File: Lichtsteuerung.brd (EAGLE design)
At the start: 157.7 x 86.4 mm, 137 parts, among them IC1 74HC595D, IC10 TSR_1-2450, IC11 MEGA64-A, IC12 75176AD, IC13 DS1307SO8, IC2 74HC595D, IC3 74HC595D, IC4 74HC595D, IC5 75176AD, IC6 MEGA8-AI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

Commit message: Added another aux connector to supply SDA, SCL, +5V and GND
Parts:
- added JP4: (no value), pinhead:2X03
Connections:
- new net AUXCON_23: IC11.5, JP4.5
- new net AUXCON_24: IC11.4, JP4.6
- net +5V: now also JP4.3
- net GND: now also JP4.4
- net SCL: now also JP4.2
- net SDA: now also JP4.1
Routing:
- net AUXCON_24: track 0.00 -> 32.9 mm
- net AUXCON_23: track 0.00 -> 30.7 mm
- net SDA: track 158.7 -> 181.2 mm
- net SCL: track 165.9 -> 185.8 mm
- net +5V: track 525.4 -> 535.2 mm
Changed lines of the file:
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@@
 <setting verticaltext="up"/>
 </settings>
-<grid distance="0.254" unitdist="mm" unit="mm" style="lines" multiple="5" display="yes" altdistance="1.27" altunitdist="mm" altunit="mm"/>
+<grid distance="0.254" unitdist="mm" unit="mil" style="lines" multiple="5" display="yes" altdistance="1.27" altunitdist="mm" altunit="mm"/>
 <layers>
 <layer number="1" name="Top" color="4" fill="1" visible="no" active="yes"/>
@@
 <text x="7.7" y="4.2" size="1.016" layer="25" rot="R90">Digital Outputs</text>
 <text x="60.9" y="4.2" size="1.016" layer="25" rot="R90">Digital Outputs</text>
-<rectangle x1="106.688" y1="27.868" x2="107.038" y2="29.268" layer="25" rot="R180"/>
-<rectangle x1="96.538" y1="31.718" x2="96.888" y2="33.118" layer="25" rot="R180"/>
-<rectangle x1="101.088" y1="30.318" x2="101.438" y2="30.668" layer="25" rot="R180"/>
-<rectangle x1="102.488" y1="25.768" x2="103.538" y2="26.118" layer="25" rot="R180"/>
-<rectangle x1="102.488" y1="26.118" x2="102.838" y2="26.818" layer="25" rot="R180"/>
-<rectangle x1="102.838" y1="26.468" x2="103.538" y2="26.818" layer="25" rot="R180"/>
-<rectangle x1="103.188" y1="26.818" x2="103.538" y2="27.518" layer="25" rot="R180"/>
-<rectangle x1="102.488" y1="27.168" x2="103.188" y2="27.518" layer="25" rot="R180"/>
-<rectangle x1="101.438" y1="26.118" x2="101.788" y2="26.468" layer="25" rot="R180"/>
-<rectangle x1="101.438" y1="26.818" x2="101.788" y2="27.168" layer="25" rot="R180"/>
-<rectangle x1="100.388" y1="25.768" x2="100.738" y2="27.518" layer="25" rot="R180"/>
-<rectangle x1="95.838" y1="24.718" x2="107.738" y2="25.068" layer="25" rot="R180"/>
-<rectangle x1="95.488" y1="34.168" x2="108.088" y2="34.518" layer="25" rot="R180"/>
-<rectangle x1="107.738" y1="24.718" x2="108.088" y2="34.168" layer="25" rot="R180"/>
-<rectangle x1="95.488" y1="24.718" x2="95.838" y2="34.168" layer="25" rot="R180"/>
+<rectangle x1="146.009" y1="35.043" x2="146.359" y2="36.443" layer="25" rot="R270"/>
+<rectangle x1="142.159" y1="24.893" x2="142.509" y2="26.293" layer="25" rot="R270"/>
+<rectangle x1="144.084" y1="29.968" x2="144.434" y2="30.318" layer="25" rot="R270"/>
+<rectangle x1="148.284" y1="31.718" x2="149.334" y2="32.068" layer="25" rot="R270"/>
+<rectangle x1="148.109" y1="31.193" x2="148.459" y2="31.893" layer="25" rot="R270"/>
+<rectangle x1="147.759" y1="31.893" x2="148.459" y2="32.243" layer="25" rot="R270"/>
+<rectangle x1="147.409" y1="31.893" x2="147.759" y2="32.593" layer="25" rot="R270"/>
+<rectangle x1="147.059" y1="31.543" x2="147.759" y2="31.893" layer="25" rot="R270"/>
+<rectangle x1="148.284" y1="30.318" x2="148.634" y2="30.668" layer="25" rot="R270"/>
+<rectangle x1="147.584" y1="30.318" x2="147.934" y2="30.668" layer="25" rot="R270"/>
+<rectangle x1="147.934" y1="28.568" x2="148.284" y2="30.318" layer="25" rot="R270"/>
+<rectangle x1="143.909" y1="30.493" x2="155.809" y2="30.843" layer="25" rot="R270"/>
+<rectangle x1="134.109" y1="30.493" x2="146.709" y2="30.843" layer="25" rot="R270"/>
+<rectangle x1="145.134" y1="32.068" x2="145.484" y2="41.518" layer="25" rot="R270"/>
+<rectangle x1="145.134" y1="19.818" x2="145.484" y2="29.268" layer="25" rot="R270"/>
 <rectangle x1="4.2" y1="37.1" x2="5.95" y2="37.45" layer="26"/>
 <rectangle x1="5.95" y1="36.75" x2="6.65" y2="37.1" layer="26"/>
@@
 <element name="F5" library="ptc-littlefuse" package="1812L" value="500mA" x="153" y="15" rot="MR270"/>
 <element name="C21" library="resistor" package="C0805" value="100n" x="135.636" y="42.164" rot="R180"/>
+<element name="JP4" library="pinhead" package="2X03" value="" x="97.79" y="27.94" rot="R270"/>
 </elements>
 <signals>
@@
 <via x="67.31" y="41.91" extent="1-16" drill="0.6"/>
 <contactref element="C21" pad="1"/>
+<contactref element="JP4" pad="4"/>
 </signal>
 <signal name="N$36">
@@
 <wire x1="134.874" y1="40.894" x2="134.874" y2="42.076" width="0.3048" layer="1"/>
 <wire x1="134.874" y1="42.076" x2="134.786" y2="42.164" width="0.3048" layer="1"/>
+<contactref element="JP4" pad="3"/>
+<wire x1="92.925" y1="34.925" x2="92.925" y2="29.249" width="0.4064" layer="1"/>
+<wire x1="92.925" y1="29.249" x2="94.234" y2="27.94" width="0.4064" layer="1"/>
+<wire x1="94.234" y1="27.94" x2="96.52" y2="27.94" width="0.4064" layer="1"/>
 </signal>
 <signal name="SR_SCK">
@@
 <wire x1="81.915" y1="44.7675" x2="81.362828125" y2="44.7675" width="0.3048" layer="16"/>
 <wire x1="81.362828125" y1="44.7675" x2="79.982103125" y2="46.148225" width="0.3048" layer="16"/>
-<wire x1="81.915" y1="44.7675" x2="86.36" y2="44.7675" width="0.3048" layer="16"/>
-<wire x1="86.36" y1="44.7675" x2="86.995" y2="43.815" width="0.3048" layer="16"/>
+<wire x1="81.915" y1="44.7675" x2="86.106" y2="44.7675" width="0.3048" layer="16"/>
+<wire x1="86.106" y1="44.7675" x2="86.995" y2="43.815" width="0.3048" layer="16"/>
 <wire x1="86.995" y1="43.815" x2="86.995" y2="40.9575" width="0.3048" layer="16"/>
 <via x="86.995" y="40.9575" extent="1-16" drill="0.6"/>
@@
 <wire x1="74.93" y1="52.3875" x2="74.93" y2="46.355" width="0.3048" layer="1"/>
 <wire x1="72.39" y1="47.625" x2="72.39" y2="48.26" width="0.3048" layer="1"/>
+<contactref element="JP4" pad="2"/>
+<wire x1="94.615" y1="48.5775" x2="94.615" y2="43.053" width="0.3048" layer="16"/>
+<wire x1="94.615" y1="43.053" x2="99.06" y2="38.608" width="0.3048" layer="16"/>
+<wire x1="99.06" y1="38.608" x2="99.06" y2="30.48" width="0.3048" layer="16"/>
 </signal>
 <signal name="SDA">
@@
 <wire x1="68.58" y1="51.7525" x2="67.945" y2="52.3875" width="0.3048" layer="1"/>
 <wire x1="67.945" y1="52.3875" x2="61.2775" y2="52.3875" width="0.3048" layer="1"/>
+<contactref element="JP4" pad="1"/>
+<wire x1="96.52" y1="30.48" x2="96.52" y2="37.592" width="0.3048" layer="16"/>
+<wire x1="96.52" y1="37.592" x2="88.138" y2="45.974" width="0.3048" layer="16"/>
+<wire x1="88.138" y1="45.974" x2="88.138" y2="46.99" width="0.3048" layer="16"/>
+<wire x1="88.138" y1="46.99" x2="88.392" y2="47.244" width="0.3048" layer="16"/>
+<wire x1="88.392" y1="47.244" x2="90.424" y2="47.244" width="0.3048" layer="16"/>
+<wire x1="90.424" y1="47.244" x2="90.4875" y2="47.3075" width="0.3048" layer="16"/>
 </signal>
 <signal name="N$42">
@@
 <wire x1="149.33" y1="12.84" x2="149.1" y2="12.61" width="0.508" layer="16"/>
 </signal>
+<signal name="AUXCON_23">
+<contactref element="IC11" pad="5"/>
+<contactref element="JP4" pad="5"/>
+<wire x1="81.095653125" y1="47.261778125" x2="81.095653125" y2="47.174346875" width="0.3048" layer="16"/>
+<wire x1="81.095653125" y1="47.174346875" x2="82.55" y2="45.72" width="0.3048" layer="16"/>
+<wire x1="82.55" y1="45.72" x2="86.106" y2="45.72" width="0.3048" layer="16"/>
+<wire x1="86.106" y1="45.72" x2="87.122" y2="44.704" width="0.3048" layer="16"/>
+<wire x1="87.122" y1="44.704" x2="87.884" y2="43.942" width="0.3048" layer="16"/>
+<wire x1="87.884" y1="43.942" x2="87.884" y2="39.37" width="0.3048" layer="16"/>
+<wire x1="87.884" y1="39.37" x2="92.202" y2="35.052" width="0.3048" layer="16"/>
+<wire x1="92.202" y1="35.052" x2="92.202" y2="29.21" width="0.3048" layer="16"/>
+<wire x1="92.202" y1="29.21" x2="95.758" y2="25.4" width="0.3048" layer="16"/>
+<wire x1="95.758" y1="25.4" x2="96.52" y2="25.4" width="0.3048" layer="16"/>
+</signal>
+<signal name="AUXCON_24">
+<contactref element="IC11" pad="4"/>
+<contactref element="JP4" pad="6"/>
+<wire x1="81.652428125" y1="47.818553125" x2="81.721446875" y2="47.818553125" width="0.3048" layer="16"/>
+<wire x1="81.721446875" y1="47.818553125" x2="83.058" y2="46.482" width="0.3048" layer="16"/>
+<wire x1="83.058" y1="46.482" x2="86.614" y2="46.482" width="0.3048" layer="16"/>
+<wire x1="86.614" y1="46.482" x2="88.646" y2="44.45" width="0.3048" layer="16"/>
+<wire x1="88.646" y1="44.45" x2="88.646" y2="39.878" width="0.3048" layer="16"/>
+<wire x1="88.646" y1="39.878" x2="93.472" y2="35.052" width="0.3048" layer="16"/>
+<wire x1="93.472" y1="35.052" x2="93.472" y2="29.21" width="0.3048" layer="16"/>
+<wire x1="93.472" y1="29.21" x2="95.758" y2="26.67" width="0.3048" layer="16"/>
+<wire x1="95.758" y1="26.67" x2="97.79" y2="26.67" width="0.3048" layer="16"/>
+<wire x1="97.79" y1="26.67" x2="99.06" y2="25.4" width="0.3048" layer="16"/>
+</signal>
 </signals>

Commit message: - Added GND for I²C connector - Added LEDs for power indication - Added output enable for shift registers - Moved pin headers to make room for cable - Added pullup/pulldown resistors and SMD jumpers to configure DMX line termination
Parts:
- added JP11, JP12, JP13, JP5, JP6, JP7: (no value), SparkFun:SJ_2S
- added LED1: 24V, led:CHIP-LED0805
- added LED2: 5V, led:CHIP-LED0805
- added R10: 220, rcl:R0805
- added R11: 10k, resistor:R0805
- added R12, R17: 120, rcl:R0805
- added R13, R14, R15, R16: 680, rcl:R0805
- added R9: 1,5k, rcl:R0805
- X7: value 733-332 -> 733-333; device con-wago_2.5mm:P-733-332 -> con-wago_2.5mm:P-733-333
- moved C9 10.7 mm to (44.5, 57.9), turned to 270 degrees
- moved C22 8.86 mm to (7.58, 44.8)
- moved C13 5.59 mm to (45.6, 44.3), turned to 90 degrees
- moved C19 4.00 mm to (17.8, 49.3)
- moved F2 2.91 mm to (41.9, 69.8), flipped to the top, turned to 180 degrees
- moved JP3 2.54 mm to (52.1, 36.8)
- moved JP4 2.54 mm to (97.8, 30.5)
- moved X8 1.27 mm to (6.35, 80.5)
- moved X3 1.27 mm to (17.8, 80.5)
- moved X6 1.27 mm to (41.9, 80.5)
- moved C5 0.17 mm to (10.0, 35.5)
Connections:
- removed net AUXCON_17: IC11.15
- removed net AUXCON_18: IC11.16
- removed net AUXCON_19: IC11.17
- removed net AUXCON_20: IC11.33
- removed net AUXCON_21: IC11.34
- removed net AUXCON_22: IC11.43
- removed net N$73: IC12.7, L1.3
- removed net N$79: IC5.7, L2.3
- new net N$101: IC12.7, L1.3, R12.2, R14.2
- new net N$80: LED1.C, R9.2
- new net N$82: LED2.C, R10.2
- new net N$85: JP12.2, R13.2
- new net N$86: JP13.1, R14.1
- new net N$88: IC5.7, L2.3, R15.1, R17.2
- new net N$89: JP11.2, R12.1
- new net N$91: JP5.1, R15.2
- new net N$92: JP7.2, R17.1
- new net N$94: JP6.2, R16.2
- new net OE: IC1.13, IC11.15, IC2.13, IC3.13, IC4.13, R11.1
- net +24V: now also LED1.A
- net +5V: now also LED2.A, R11.2
- net GND: now also R10.1, R9.1, X7.L3; no longer IC1.13, IC2.13, IC3.13, IC4.13
- net GNDI1: now also JP13.2
- net GNDI2: now also JP5.2
- net N$53: now also JP11.1, R13.1
- net N$77: now also JP7.1, R16.1
- net VCCIO1: now also JP12.1
- net VCCIO2: now also JP6.1
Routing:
- net OE: track 0.00 -> 108.6 mm, vias 0 -> 7
- net N$53: track 2.94 -> 21.2 mm, vias 0 -> 1
- net GNDI2: track 45.5 -> 62.9 mm
- net +24V: track 213.0 -> 229.7 mm
- net VCCIO2: track 27.1 -> 41.7 mm, vias 0 -> 1
- net GNDI1: track 45.3 -> 58.4 mm
- net N$77: track 2.91 -> 14.9 mm, vias 0 -> 1
- net VCCIO1: track 27.5 -> 38.7 mm, vias 0 -> 1
- net N$88: track 0.00 -> 9.85 mm, vias 0 -> 1
- net N$101: track 0.00 -> 9.79 mm, vias 0 -> 1
- net SDA: track 181.2 -> 171.6 mm
- net SCL: track 185.8 -> 177.6 mm
- net +5V: track 535.2 -> 543.3 mm
- net N$80: track 0.00 -> 6.59 mm
- net N$82: track 0.00 -> 6.38 mm
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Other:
- board text added: "RZL Lichtsteuerung Revishiun C"
- board text removed: "RaumZeitLabor Lichtsteuerung Rev. B"

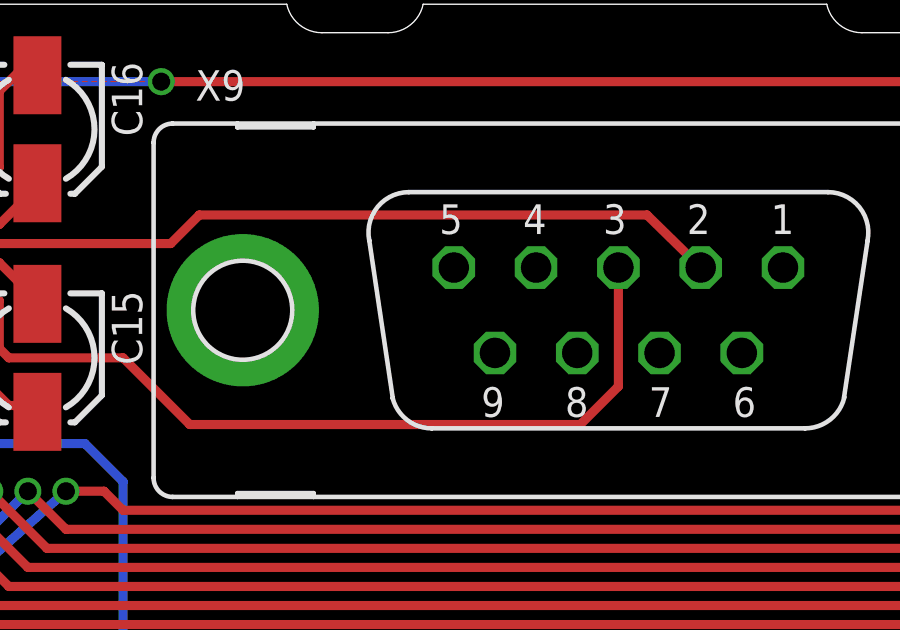
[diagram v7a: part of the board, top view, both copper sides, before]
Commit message: Swapped RXD and TXD, because this is a DCE, not a DTE. In plain words: You can simply connect any USB-RS232 connector to the port now, instead of using a null modem cable with crossed RXD/TXD pairs.
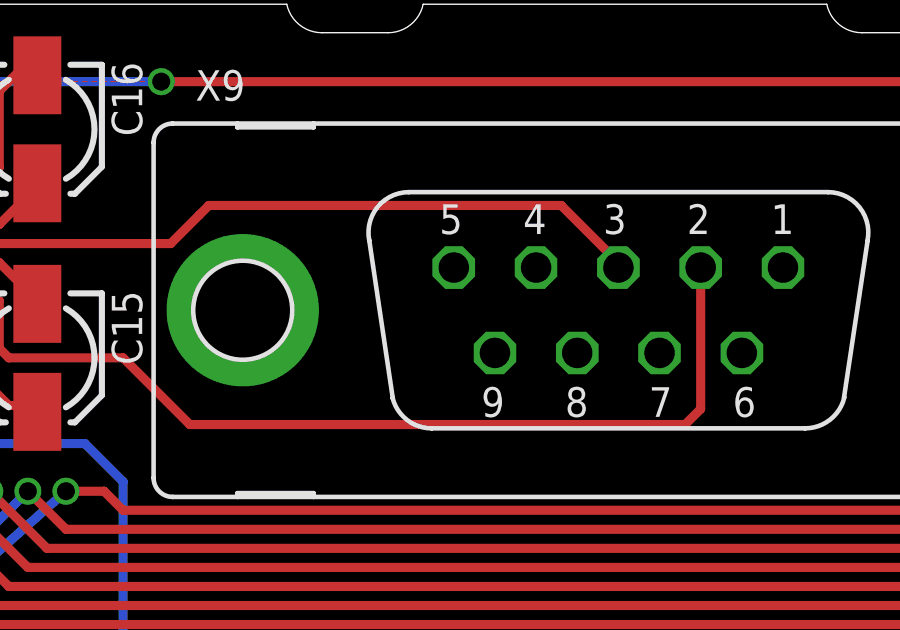
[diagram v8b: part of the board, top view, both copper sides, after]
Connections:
- net RS232_RXD: now also X9.3; no longer X9.2
- net RS232_TXD: now also X9.2; no longer X9.3
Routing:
- net RS232_TXD: track 35.5 -> 38.7 mm
- net RS232_RXD: track 32.0 -> 29.6 mm
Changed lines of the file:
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@@
 <signal name="RS232_RXD">
 <contactref element="U1" pad="13"/>
-<contactref element="X9" pad="2"/>
 <wire x1="59.7475" y1="79.0575" x2="61.2775" y2="79.0575" width="0.3048" layer="1"/>
 <wire x1="61.2775" y1="79.0575" x2="61.9125" y2="78.4225" width="0.3048" layer="1"/>
 <wire x1="61.9125" y1="78.4225" x2="72.7075" y2="78.4225" width="0.3048" layer="1"/>
 <wire x1="72.7075" y1="78.4225" x2="73.66" y2="79.375" width="0.3048" layer="1"/>
-<wire x1="73.66" y1="79.375" x2="88.5825" y2="79.375" width="0.3048" layer="1"/>
-<wire x1="88.5825" y1="79.375" x2="90.3732" y2="77.6224" width="0.3048" layer="1"/>
+<contactref element="X9" pad="3"/>
+<wire x1="87.63" y1="77.6224" x2="87.63" y2="77.7875" width="0.3048" layer="1"/>
+<wire x1="87.63" y1="77.7875" x2="85.725" y2="79.6925" width="0.3048" layer="1"/>
+<wire x1="85.725" y1="79.6925" x2="73.9775" y2="79.6925" width="0.3048" layer="1"/>
+<wire x1="73.9775" y1="79.6925" x2="73.66" y2="79.375" width="0.3048" layer="1"/>
 </signal>
 <signal name="RS232_TXD">
 <contactref element="U1" pad="14"/>
-<contactref element="X9" pad="3"/>
 <wire x1="59.7475" y1="77.7875" x2="63.8175" y2="77.7875" width="0.3048" layer="1"/>
 <wire x1="63.8175" y1="77.7875" x2="64.4525" y2="77.1525" width="0.3048" layer="1"/>
@@
 <wire x1="71.12" y1="74.6125" x2="73.3425" y2="72.39" width="0.3048" layer="1"/>
 <wire x1="73.3425" y1="72.39" x2="86.36" y2="72.39" width="0.3048" layer="1"/>
-<wire x1="86.36" y1="72.39" x2="87.63" y2="73.66" width="0.3048" layer="1"/>
-<wire x1="87.63" y1="73.66" x2="87.63" y2="77.6224" width="0.3048" layer="1"/>
+<contactref element="X9" pad="2"/>
+<wire x1="90.3732" y1="77.6224" x2="90.3732" y2="72.9107" width="0.3048" layer="1"/>
+<wire x1="90.3732" y1="72.9107" x2="89.8525" y2="72.39" width="0.3048" layer="1"/>
+<wire x1="89.8525" y1="72.39" x2="86.36" y2="72.39" width="0.3048" layer="1"/>
 </signal>
 <signal name="N$156">
